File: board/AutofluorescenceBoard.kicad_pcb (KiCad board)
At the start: 2 copper layers, 65.8 x 53.7 mm, 45 parts, among them J1 2002411212, Q1 BSS138, U1 PAM2863ECR, U2 PAM2863ECR, U3 PAM2863ECR

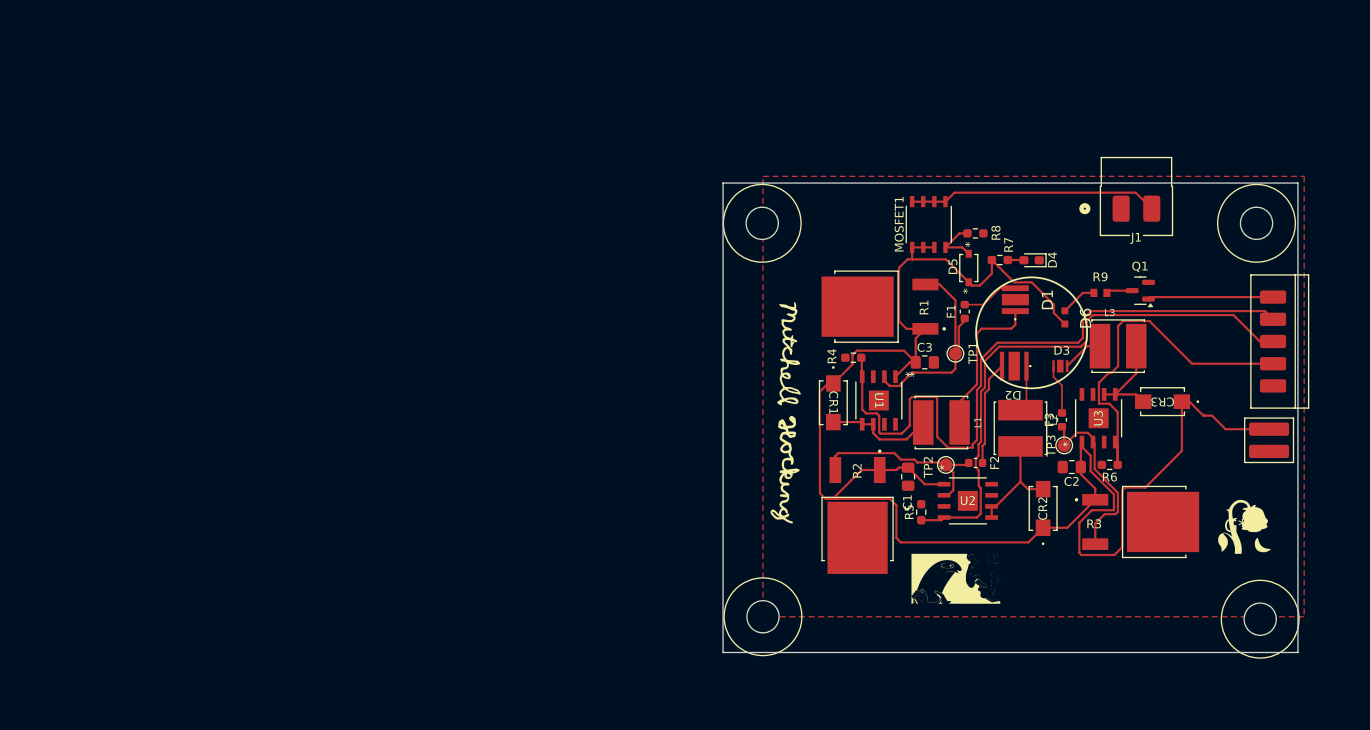
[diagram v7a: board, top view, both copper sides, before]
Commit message: Finished up
adjust mounting holes and light sealable space
no 90 degrees
Trace width 12 V 5A
Add silkscreen documentation
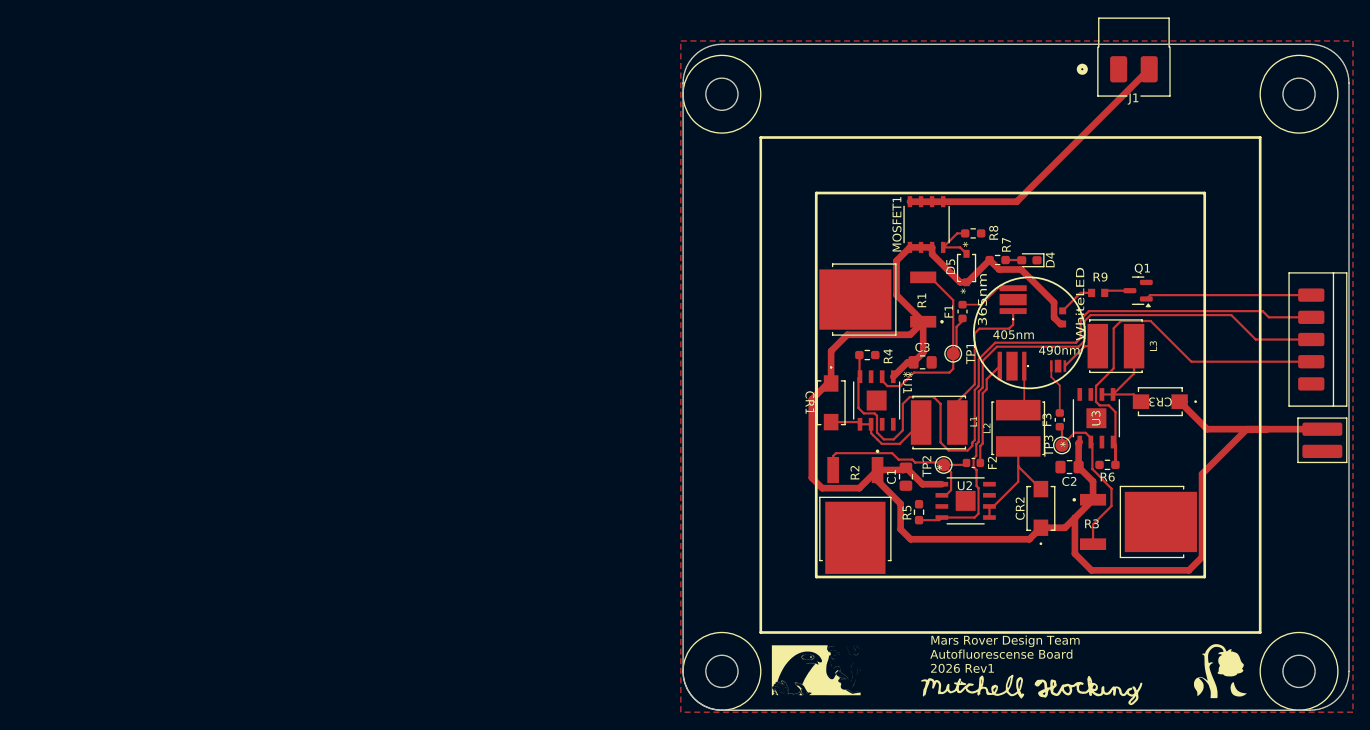
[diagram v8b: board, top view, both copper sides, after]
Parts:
- moved G*** 42.1 mm to (181.4, 150.6), turned to 0 degrees
- moved G*** 19.1 mm to (156.5, 148.6)
- moved G*** 16.7 mm to (202.7, 148.6)
- moved J1 16.0 mm to (191.1, 79.8)
- moved H1 15.6 mm to (207.3, 87.1)
- moved H2 15.5 mm to (150.1, 87.1)
- moved H4 7.82 mm to (141.2, 153.2)
- moved H3 7.44 mm to (207.3, 144.3)
- moved FanConn1 6.10 mm to (215.9, 121.0)
- moved Conn1 4.37 mm to (213.1, 105.7)
- moved R4 1.63 mm to (162.3, 112.5), turned to 0 degrees
- moved R1 0.85 mm to (163.5, 106.2)
- moved 365nm 0.25 mm to (179.0, 106.2)
- moved C1 0.25 mm to (166.7, 126.4)
- moved C2 0.25 mm to (185.4, 125.3)
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- renumbered D1 to 365nm, D2 to 405nm, D3 to 490nm, D6 to WhiteLED
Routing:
- net ISET 365nm: track 77.4 -> 82.8 mm
- net Net-(J1-Pad2): track 28.6 -> 33.7 mm
- net White LED: track 14.3 -> 19.1 mm
- net ISET 405nm: track 63.0 -> 67.5 mm
- net ISET 490nm: track 41.3 -> 45.6 mm
- net +12V: track 188.4 -> 186.9 mm
- net Net-(U3-ISENSE): track 21.9 -> 20.7 mm
- net Net-(CR2-Pad2): track 12.7 -> 13.5 mm
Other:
- board size 65.8 x 53.7 mm -> 76.2 x 76.2 mm
- board text added: "Mars Rover Design Team Autofluorescense Board 2026 Rev1"
